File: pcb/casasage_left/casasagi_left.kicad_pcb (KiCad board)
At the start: 2 copper layers, 132.2 x 83.2 mm, 113 parts, among them J1 USB_C_Receptacle_USB2.0, J2 AudioJack4, J3 Conn_01x05, SW1 RESET, SW2 BOOT, U1 TLV73333PDBV, U2 STM32F072C8Tx, U3 AT24CS32-XHM, Y1 8MHz

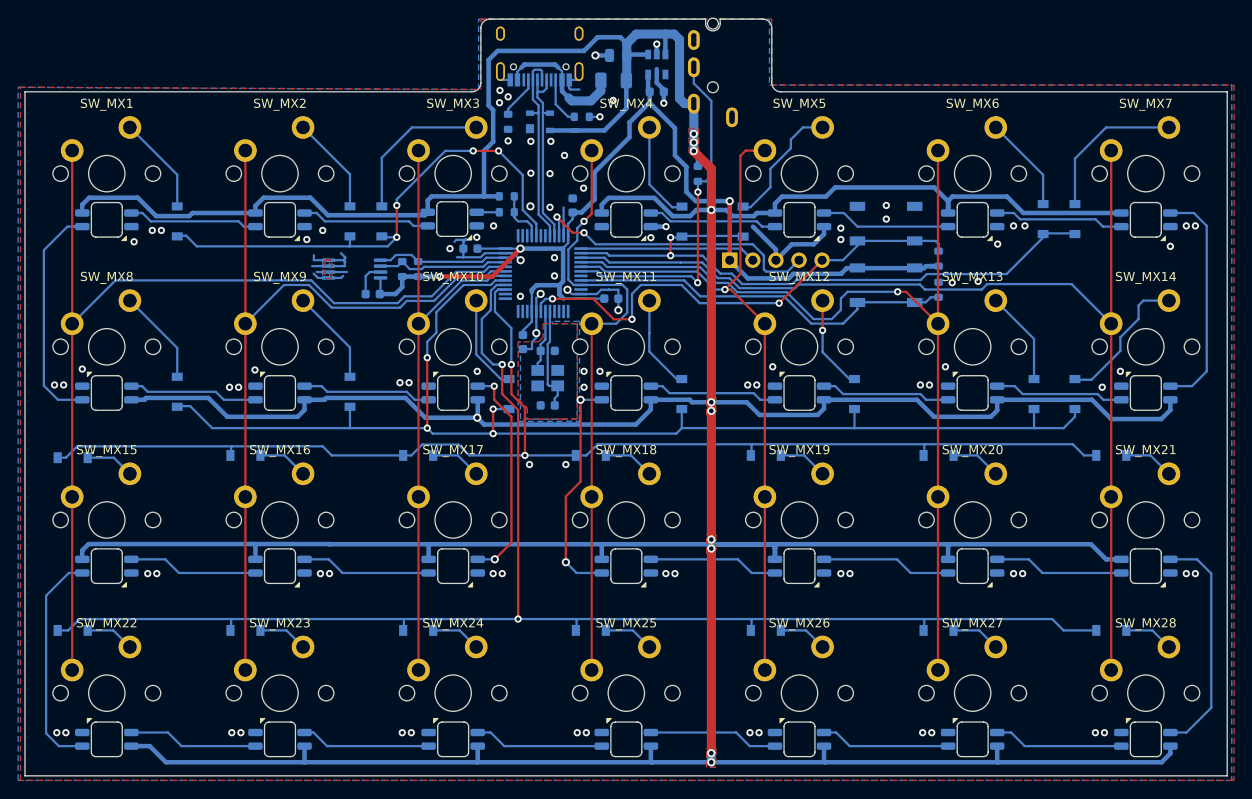
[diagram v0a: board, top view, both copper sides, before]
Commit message: change pcb outline
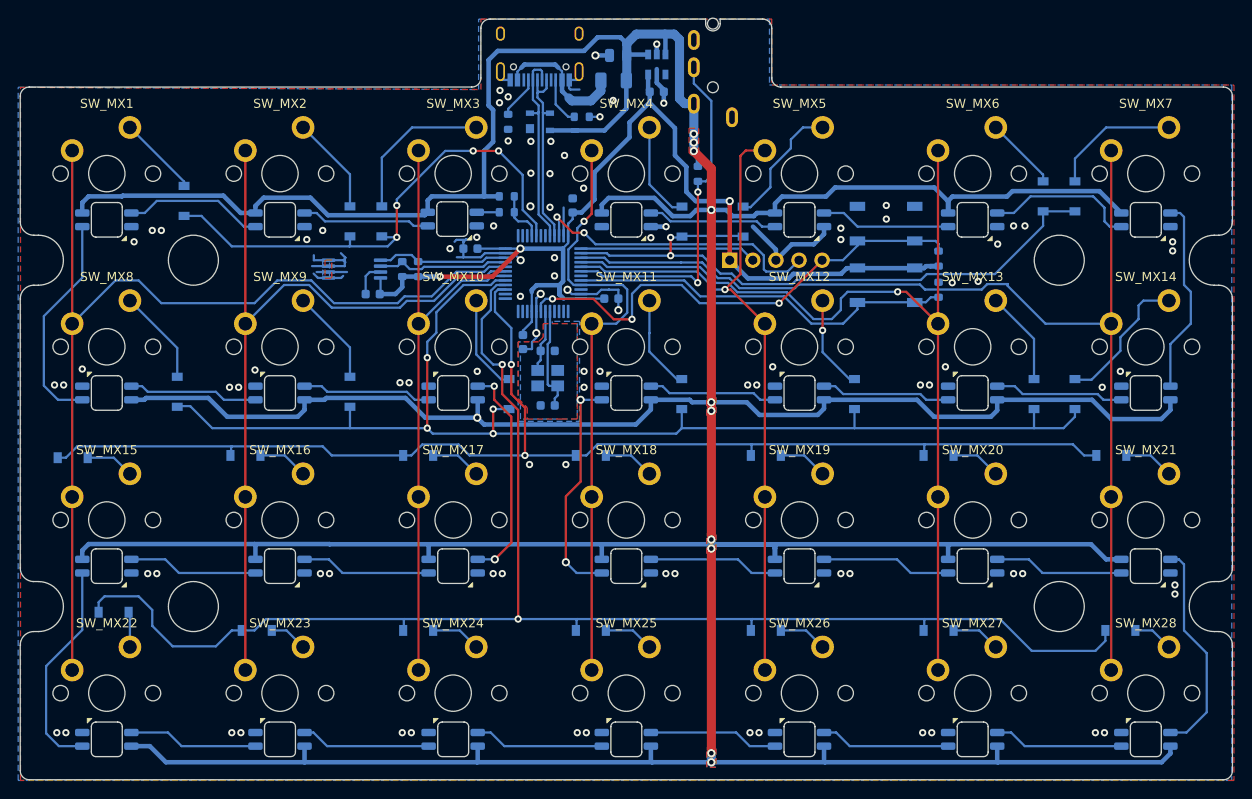
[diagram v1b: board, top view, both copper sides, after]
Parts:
- moved D23 4.92 mm to (50.8, 98.2)
- moved D7 2.50 mm to (153.0, 52.5)
- moved D8 2.50 mm to (156.5, 52.5)
- moved D2 2.37 mm to (58.5, 53.0)
- moved D24 1.25 mm to (66.5, 100.2)
- moved D29 1.00 mm to (161.5, 100.2)
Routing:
- net Net-(LED24-Pad2): track 25.3 -> 21.5 mm
- net /ROW4: track 162.3 -> 165.5 mm
- net Net-(D8-Pad2): track 16.8 -> 14.3 mm
- net Net-(D7-Pad2): track 10.7 -> 8.09 mm
- net Net-(LED25-Pad2): track 14.3 -> 16.7 mm
- net /COL0: track 109.5 -> 111.5 mm
- net Net-(D2-Pad2): track 10.9 -> 8.90 mm
- net Net-(LED3-Pad2): track 26.0 -> 24.1 mm
- net /ROW1: track 68.4 -> 70.0 mm
- net Net-(D23-Pad2): track 5.47 -> 3.88 mm
- net Net-(LED16-Pad2): track 25.5 -> 23.9 mm
- net Net-(D24-Pad2): track 5.52 -> 4.19 mm
- net Net-(LED2-Pad2): track 14.3 -> 15.4 mm
- net Net-(D29-Pad2): track 5.52 -> 4.44 mm
- net Net-(LED10-Pad4): track 24.7 -> 23.8 mm
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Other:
- board size 132.2 x 83.2 mm -> 133.3 x 83.7 mm

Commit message: replace stm32f072 symbol to kicad pre-installed one
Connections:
- J1 pad A8: Net-(J1-PadA8) -> (no net)
- J1 pad B8: Net-(J1-PadB8) -> (no net)
- J2 pad R2: Net-(J2-PadR2) -> (no net)
- LED28 pad 2: Net-(LED28-Pad2) -> (no net)
- U1 pad 4: Net-(U1-Pad4) -> (no net)
- U2 pad 1: Net-(U2-Pad1) -> (no net)
- U2 pad 10: Net-(U2-Pad10) -> (no net)
- U2 pad 11: Net-(U2-Pad11) -> (no net)
- U2 pad 12: Net-(U2-Pad12) -> (no net)
- U2 pad 13: Net-(U2-Pad13) -> (no net)
- U2 pad 14: Net-(U2-Pad14) -> (no net)
- U2 pad 2: Net-(U2-Pad2) -> (no net)
- U2 pad 25: Net-(U2-Pad25) -> (no net)
- U2 pad 26: Net-(U2-Pad26) -> (no net)
- U2 pad 27: Net-(U2-Pad27) -> (no net)
- U2 pad 3: Net-(U2-Pad3) -> (no net)
- U2 pad 30: Net-(U2-Pad30) -> (no net)
- U2 pad 31: Net-(U2-Pad31) -> (no net)
- U2 pad 4: Net-(U2-Pad4) -> (no net)
- U2 pad 43: Net-(U2-Pad43) -> (no net)
- U2 pad 46: Net-(U2-Pad46) -> (no net)
